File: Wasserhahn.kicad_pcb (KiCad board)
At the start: 2 copper layers, 90.2 x 77.5 mm, 18 parts, among them J1 Mains, J2 Ball_Valve_Contacts, J3 ToRelais, J4 PRGM_ADAPTER, J5 Boot/PRGM, U1 ESP-WROOM-02

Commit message: Updated Board and Plot data
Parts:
- J2: moved to B.Cu
- moved C4 15.3 mm to (139.7, 40.6)
- moved PS1 3.17 mm to (123.8, 82.5)
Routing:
- net /GND: track 383.6 -> 353.0 mm
- net /Input_Open: track 152.8 -> 138.4 mm
- net /VCC3V3: track 124.6 -> 118.6 mm
- net Net-(J1-Pad1): track 13.3 -> 15.4 mm
- net Net-(J1-Pad2): track 13.3 -> 14.7 mm
- net /Input_Close: track 55.8 -> 56.8 mm
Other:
- board size 90.2 x 77.5 mm -> 76.2 x 78.1 mm

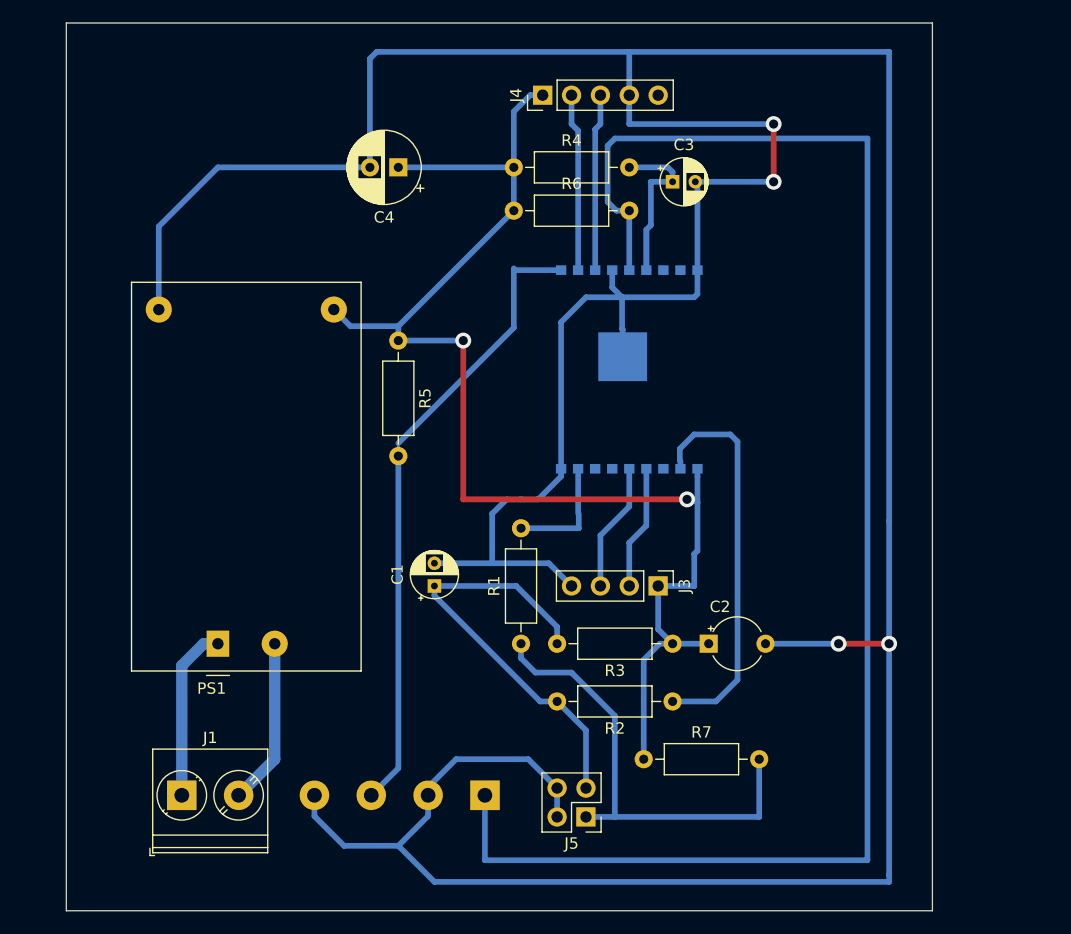
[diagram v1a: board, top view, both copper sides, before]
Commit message: optimized path in flatcam and widened the track width in kiCad
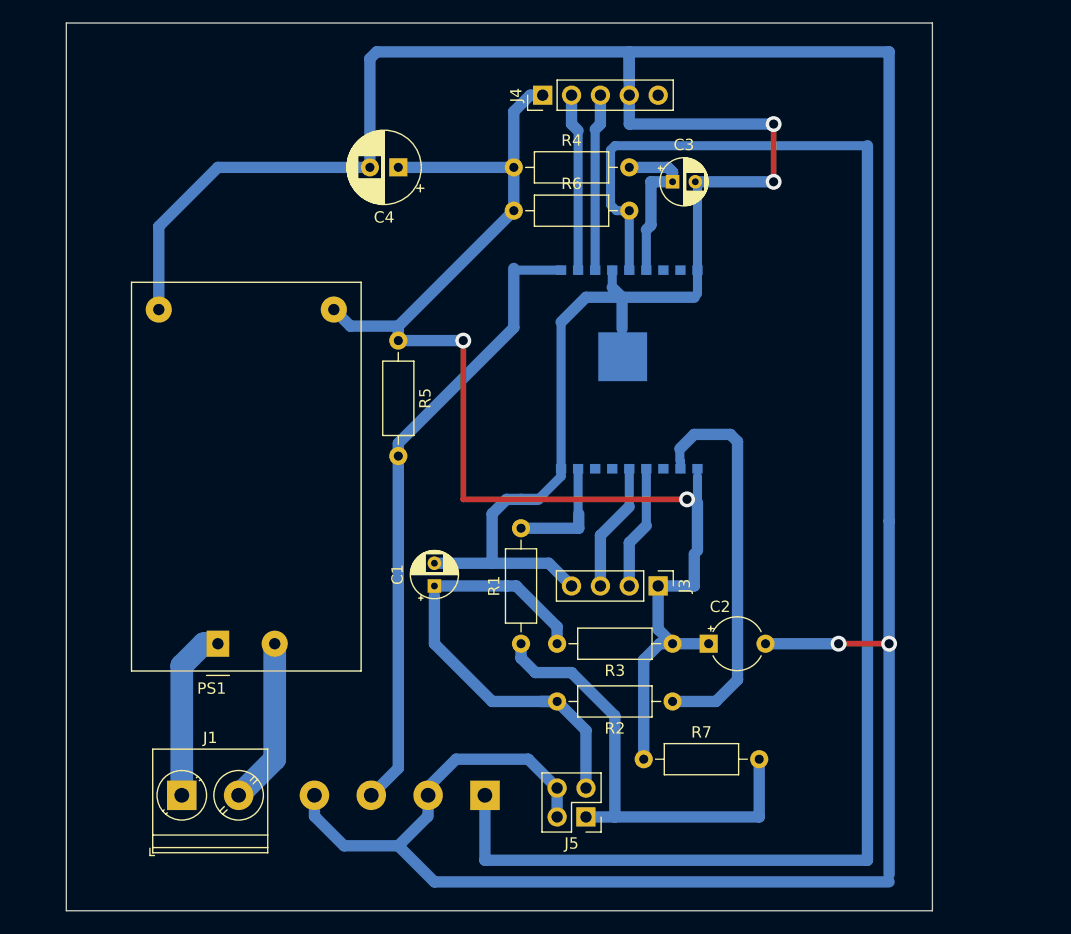
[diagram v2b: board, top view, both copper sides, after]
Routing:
- net Net-(C1-Pad1): track 37.9 -> 41.9 mm
- net /Input_Open: track 138.4 -> 136.9 mm
